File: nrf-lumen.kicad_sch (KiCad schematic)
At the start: 10 parts, among them J1 Barrel_Jack_MountingPin, J2 Conn_01x03, Q1 BSS138

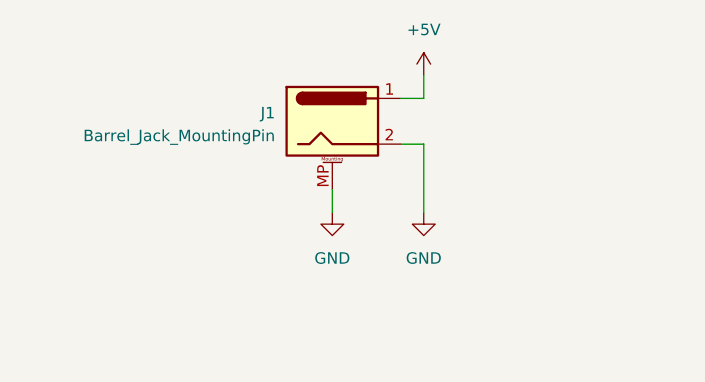
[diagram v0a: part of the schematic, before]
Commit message: Prepare for Aisler assembly
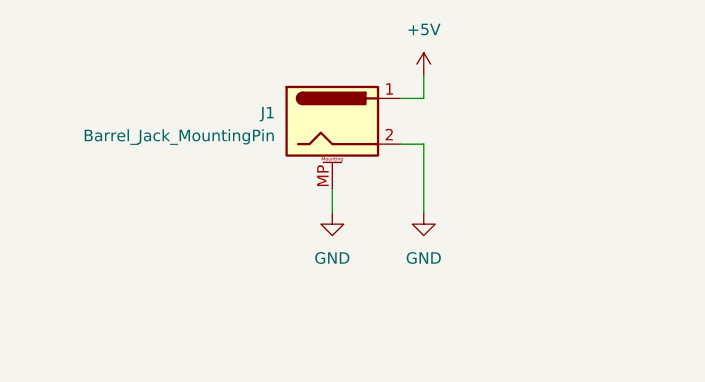
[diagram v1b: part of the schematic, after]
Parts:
- C4: MFG (none) -> KEMET; MPN (none) -> ESK108M6R3AG3AA; Mfr. KEMET -> (none); Mfr. No ESK108M6R3AG3AA -> (none); Mouser No 80-ESK108M6R3AG3AA -> (none); Order Code (none) -> 80-ESK108M6R3AG3AA
- J1: MFG (none) -> CUI Devices; MPN (none) -> PJ-063AH; Mfr. CUI Devices -> (none); Mfr. No PJ-063AH -> (none); Mouser No 490-PJ-063AH -> (none); Order Code (none) -> 490-PJ-063AH
- J2: MFG (none) -> SparkFun; MPN (none) -> PRT-09750; Mfr. SparkFun -> (none); Mfr. No PRT-09750 -> (none); Mouser No 474-PRT-09750 -> (none); Order Code (none) -> 474-PRT-09750
- Q1: MFG (none) -> Diodes Incorporated; MPN (none) -> BSS138-7-F; Mfr. Diodes Incorporated -> (none); Mfr. No BSS138-7-F -> (none); Mouser No 621-BSS138-7-F -> (none); Order Code (none) -> 621-BSS138-7-F
- R2, R3: MFG (none) -> YAGEO; MPN (none) -> RC0402FR-0710KL; Mfr. YAGEO -> (none); Mfr. No RC0402FR-0710KL -> (none); Mouser No 603-RC0402FR-0710KL -> (none); Order Code (none) -> 603-RC0402FR-0710KL
